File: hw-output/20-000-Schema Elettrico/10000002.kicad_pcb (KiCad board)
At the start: 4 copper layers, 45.7 x 32 mm, 31 parts, among them P1 CONN_4, P2 CONN_4, P3 CONN_4, P4 CONN_4, P5 CONN_4, P6 CONN_4, P7 CONN_4, P8 CONN_4, U1 PCF8574, U2 AQZ204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

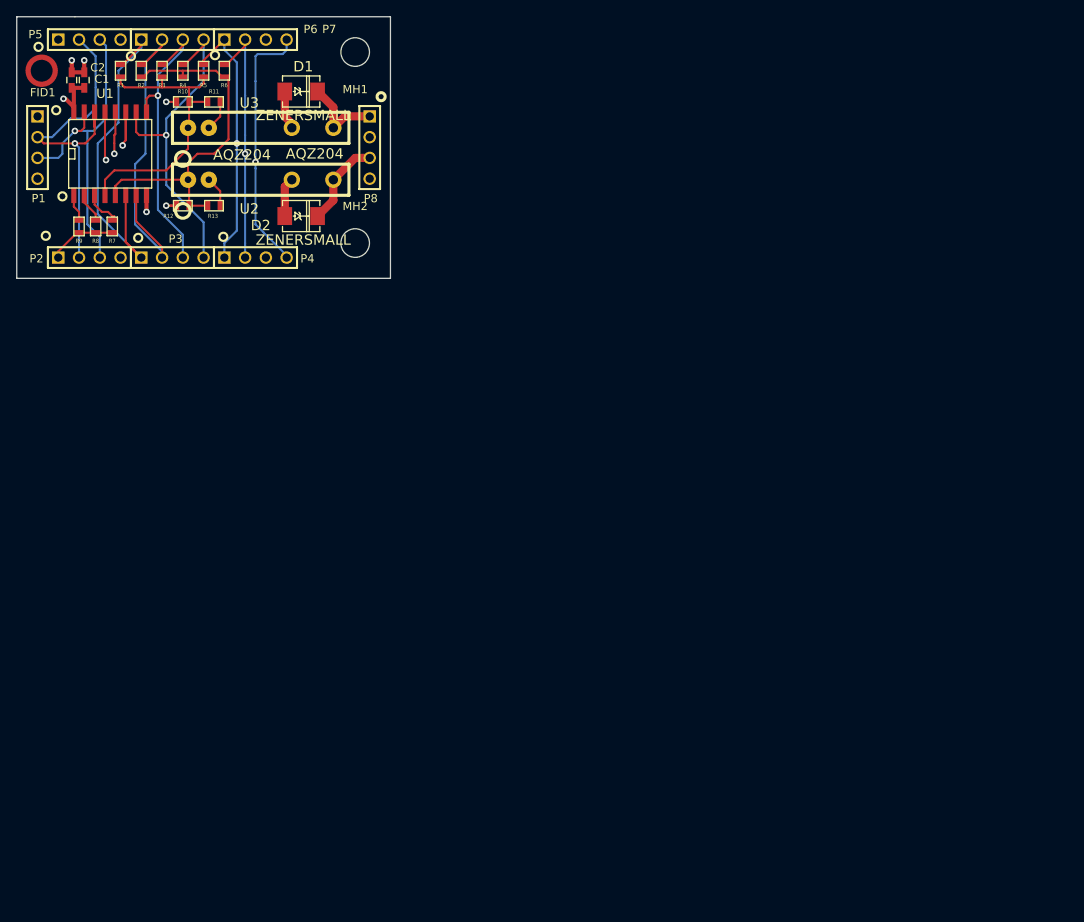
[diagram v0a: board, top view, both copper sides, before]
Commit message: Completato schema e sbroglio
Signed-off-by: CrazyDiamond <crazyd14@gmail.com>
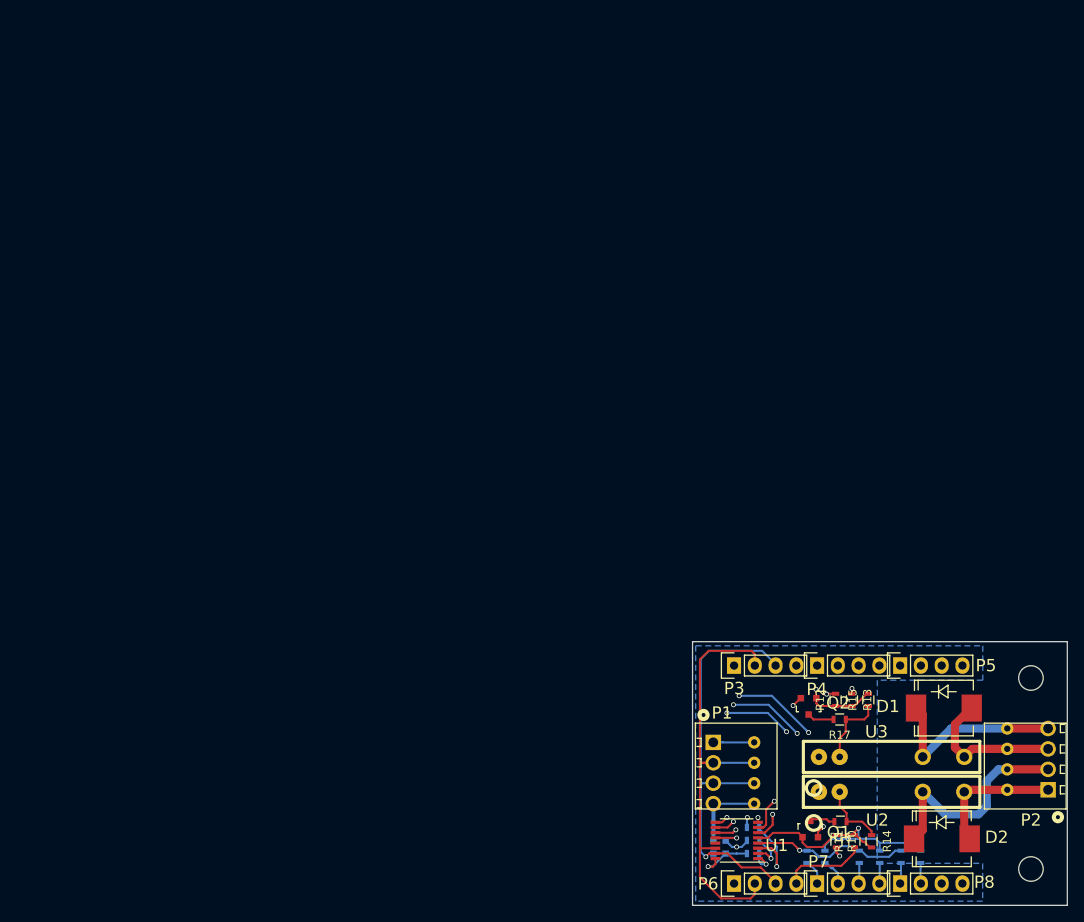
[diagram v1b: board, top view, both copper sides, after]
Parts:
- removed FID1: Fiducial_Modern_CopperTop, Fiducials:Fiducial_Modern_CopperTop
- removed MH1, MH2: MountingHole_3-5mm, Mounting_Holes:MountingHole_3-5mm
- added Q1: Q_PMOS_GSD_BSS84, TO_SOT_Packages_SMD:SOT-23, F.Cu at (180.9, 142.3)
- added Q2: Q_PMOS_GSD_BSS84, TO_SOT_Packages_SMD:SOT-23, F.Cu at (180.7, 127.3)
- added R14: R_1K_0603_5, Resistors_SMD:R_0603, F.Cu at (188.4, 143.8)
- added R15: R_1K_0603_5, Resistors_SMD:R_0603, F.Cu at (188.0, 126.5)
- added R16: R_1K_0603_5, Resistors_SMD:R_0603, F.Cu at (184.6, 141.4)
- added R17: R_1K_0603_5, Resistors_SMD:R_0603, F.Cu at (184.5, 128.9)
- added REF**: MountingHole_3mm, Mounting_Holes:MountingHole_3mm, F.Cu at (207.9, 123.8)
- added REF**: MountingHole_3mm, Mounting_Holes:MountingHole_3mm, F.Cu at (207.9, 147.2)
- C1: value 100n -> C_100n_0603_10_X7R_25V; footprint Capacitors_SMD:C_0603_HandSoldering -> Capacitors_SMD:C_0603; moved to B.Cu
- C2: value 1u -> C_1u_0603_10_X7R_25V; footprint Capacitors_SMD:C_0603_HandSoldering -> Capacitors_SMD:C_0603; moved to B.Cu
- D1, D2: value ZENERSMALL -> TVS_SMC_49.1V; footprint DO214 -> Diodes_SMD:SMC_Standard
- P1, P2: value CONN_4 -> TERMINAL_01X04_250_RA_SPRING; footprint PIN_ARRAY_4x1 -> os_terminal_block:1770908
- P3, P4, P5, P6, P7, P8: value CONN_4 -> PLUG_01X04_254; footprint PIN_ARRAY_4x1 -> Socket_Strips:Socket_Strip_Straight_1x04
- R1, R2, R3, R4, R5, R6: value 0 -> R_0_0603_5; footprint SM0603 -> Resistors_SMD:R_0603; moved to B.Cu
- R10, R12: value 1000 -> R_10K_0603_5; footprint SM0603 -> Resistors_SMD:R_0603
- R11, R13: value 10000 -> R_10K_0603_5; footprint SM0603 -> Resistors_SMD:R_0603
- R7, R8, R9: value 10000 -> R_10K_0603_5; footprint SM0603 -> Resistors_SMD:R_0603; moved to B.Cu
- U1: value PCF8574 -> TCA9554; footprint SO16L -> Housings_SSOP:SSOP-16_3.9x4.9mm_Pitch0.635mm
- U2, U3: footprint AQZ-SIL-4 -> os_photomos:AQZ-SIL-4
- moved P2 134.2 mm to (210.0, 137.5), turned to 90 degrees
- moved R5 128.6 mm to (192.0, 145.7), turned to 90 degrees
- moved R3 128.5 mm to (186.9, 145.7), turned to 90 degrees
- moved R4 128.5 mm to (189.4, 145.7), turned to 90 degrees
- moved R6 128.5 mm to (194.4, 145.7), turned to 90 degrees
- moved R1 127.7 mm to (180.5, 145.7), turned to 90 degrees
- moved R2 127.5 mm to (182.7, 145.7), turned to 90 degrees
- moved P5 125.3 mm to (191.9, 122.3)
- moved P6 124.0 mm to (171.6, 149.0)
- moved P7 124.0 mm to (181.7, 149.0)
- moved C2 123.4 mm to (169.8, 145.3), turned to 180 degrees
- moved C1 121.3 mm to (169.8, 143.7), turned to 180 degrees
- moved R10 120.7 mm to (184.1, 143.8), turned to 270 degrees
- moved R11 119.7 mm to (186.3, 143.8), turned to 90 degrees
- moved U1 113.7 mm to (171.9, 143.7), turned to 180 degrees
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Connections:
- C1 pad 1: VDD -> +5V
- C2 pad 1: VDD -> +5V
- D1 pad 1: /IO_0_N -> /IO_0_P
- D1 pad 2: /IO_0_P -> /IO_0_N
- D2 pad 1: /IO_1_N -> /IO_1_P
- D2 pad 2: /IO_1_P -> /IO_1_N
- P1 pad 1: VDD -> +5V
- P2 pad 1: VDD -> /IO_1_N
- P2 pad 2: /I2C_SCL -> /IO_1_P
- P2 pad 3: /I2C_SDA -> /IO_0_N
- P2 pad 4: GND -> /IO_0_P
- P3 pad 1: /IO_2_CMD -> +5V
- P3 pad 2: /IO_3_CMD -> /I2C_SCL
- P3 pad 3: /IO_4_CMD -> /I2C_SDA
- P3 pad 4: /IO_5_CMD -> GND
- P4 pad 1: /IO_6_CMD -> /IO_2_CMD
- P4 pad 2: /IO_7_CMD -> /IO_3_CMD
- P4 pad 3: /NC1 -> /IO_4_CMD
- P4 pad 4: /I2C_INT -> /IO_5_CMD
- P5 pad 1: VDD -> /IO_6_CMD
- P5 pad 2: /I2C_SCL -> /IO_7_CMD
- P5 pad 3: /I2C_SDA -> /NC1
- P5 pad 4: GND -> /I2C_INT
- P6 pad 1: /IO_2_CMD -> +5V
- P6 pad 2: /IO_3_CMD -> /I2C_SCL
- P6 pad 3: /IO_4_CMD -> /I2C_SDA
- P6 pad 4: /IO_5_CMD -> GND
- P7 pad 1: /IO_6_CMD -> /IO_2_CMD
- P7 pad 2: /IO_7_CMD -> /IO_3_CMD
- P7 pad 3: /NC1 -> /IO_4_CMD
- P7 pad 4: /I2C_INT -> /IO_5_CMD
- P8 pad 1: /IO_0_P -> /IO_6_CMD
- P8 pad 2: /IO_0_N -> /IO_7_CMD
- P8 pad 3: /IO_1_P -> /NC1
- P8 pad 4: /IO_1_N -> /I2C_INT
- R10 pad 1: VDD -> /IO_1_CMD
- R10 pad 2: /IO_0_CMD -> +5V
- R11 pad 1: /IO_0_CMD -> GND
- R11 pad 2: GND -> /IO_1_CMD
- R12 pad 1: VDD -> /IO_0_CMD
- R12 pad 2: /IO_1_CMD -> +5V
- R13 pad 1: /IO_1_CMD -> GND
- R13 pad 2: GND -> /IO_0_CMD
- R7 pad 1: VDD -> Net-(R7-Pad1)
- R7 pad 2: Net-(R7-Pad2) -> +5V
- R8 pad 1: VDD -> Net-(R8-Pad1)
- R8 pad 2: Net-(R8-Pad2) -> +5V
- R9 pad 1: VDD -> Net-(R9-Pad1)
- R9 pad 2: Net-(R9-Pad2) -> +5V
- U1 pad 1: Net-(R9-Pad2) -> Net-(R9-Pad1)
- U1 pad 16: VDD -> +5V
- U1 pad 2: Net-(R8-Pad2) -> Net-(R8-Pad1)
- U1 pad 3: Net-(R7-Pad2) -> Net-(R7-Pad1)
- U2 pad 1: /IO_1_CMD -> GND
- U2 pad 2: GND -> Net-(R14-Pad1)
- U2 pad 3: /IO_1_N -> /IO_1_P
- U2 pad 4: /IO_1_P -> /IO_1_N
- U3 pad 1: /IO_0_CMD -> GND
- U3 pad 2: GND -> Net-(R15-Pad1)
- U3 pad 3: /IO_0_N -> /IO_0_P
- U3 pad 4: /IO_0_P -> /IO_0_N
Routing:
- net /I2C_INT: track 56.4 -> 0.00 mm, vias 2 -> 0
- net /IO_7_CMD: track 52.3 -> 87.0 mm, vias 2 -> 1
- net /IO_5_CMD: track 41.0 -> 69.6 mm, vias 1 -> 3
- net /IO_4_CMD: track 36.6 -> 61.8 mm, vias 1 -> 3
- net +5V: track 0.00 -> 22.1 mm, vias 0 -> 7
- net /IO_6_CMD: track 54.8 -> 74.5 mm, vias 2 -> 3
- net VDD: track 19.2 -> 0.00 mm, vias 3 -> 0
- net /IO_0_CMD: track 36.8 -> 51.0 mm, vias 0 -> 2
- net /I2C_SDA: track 40.7 -> 53.5 mm
- net /IO_1_P: track 15.3 -> 26.7 mm
- net /IO_0_P: track 13.0 -> 23.1 mm
- net /IO_1_CMD: track 43.6 -> 33.5 mm, vias 0 -> 1
- net Net-(R7-Pad1): track 0.00 -> 9.87 mm, vias 0 -> 1
- net /I2C_SCL: track 46.0 -> 55.7 mm, vias 1 -> 0
- net Net-(R15-Pad1): track 0.00 -> 8.99 mm
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- added copper zone on In1.Cu, net +5V
- added copper zone on B.Cu, net GND
- removed copper zone on GND, net GND
- removed copper zone on VCC, net VDD
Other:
- board size 45.7 x 32 mm -> 45.8 x 32.3 mm
- net class Default: clearance 0.254 -> 0.2; trace_width 0.127 -> 0.25; via_dia 0.8001 -> 0.6; via_drill 0.50038 -> 0.4
- rule pad_to_mask_clearance: 0.254 -> 0.2
- rule trace_clearance: 0.254 -> 0.2
- rule trace_min: 0.127 -> 0.1
- rule via_min_drill: 0.50038 -> 0.3
- rule via_min_size: 0.8001 -> 0.4
